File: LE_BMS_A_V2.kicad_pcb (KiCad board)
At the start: 4 copper layers, 80 x 80 mm, 56 parts, among them J1 10155435-00011LF, J2 CAN1, J3 691382010012, J4 691313510002, J5 RJHSE5380, J6 CAN1, U1 ESP32-S3-WROOM-2, U2 MCP2515-xST, U3 ISO1050DUB, U4 ISO1050DUB, U5 TLV1117LV33DCYT, U6 DS3231MZ, Y1 ABM3B-8.000MHZ-10-1-U-T

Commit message: Moved the PCB a bit.
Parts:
- added REF**: BatteryHolder_MYOUNG_BS-07-A1BJ001_CR2032, Battery:BatteryHolder_MYOUNG_BS-07-A1BJ001_CR2032, F.Cu at (127.2, 64.2)
- moved C5 70.8 mm to (180.1, 49.6)
- moved C6 70.8 mm to (166.1, 97.2)
- moved C7 70.8 mm to (136.1, 97.1)
- moved J6 70.8 mm to (171.3, 117.3)
- moved U2 70.8 mm to (133.1, 85.6)
- moved U4 70.8 mm to (130.3, 102.5)
- moved U6 70.8 mm to (153.4, 84.4)
- moved C1 70.8 mm to (151.8, 53.8)
- moved C10 70.8 mm to (145.7, 116.6)
- moved C12 70.8 mm to (133.2, 109.4)
- moved C13 70.8 mm to (139.0, 89.9)
- moved C14 70.8 mm to (139.0, 81.7)
- moved C15 70.8 mm to (175.0, 105.3)
- moved C17 70.8 mm to (175.0, 99.8)
- moved C18 70.8 mm to (138.8, 99.5)
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
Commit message: Finished most routing, final checks to be done
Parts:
- removed REF**: BatteryHolder_MYOUNG_BS-07-A1BJ001_CR2032, Battery:BatteryHolder_MYOUNG_BS-07-A1BJ001_CR2032
- added BT1: Battery_Cell, Battery:BatteryHolder_MYOUNG_BS-07-A1BJ001_CR2032, F.Cu at (118.1, 72.4)
- added G***: LOGO, LOGO, F.Cu at (137.7, 89.5)
- added J7: 691382010006, 691382010006:691382010006, F.Cu at (187.0, 84.1)
- J3: value 691382010012 -> 691382010006; footprint 691382010012:691382010012 -> 691382010006:691382010006
- moved C22 45.6 mm to (116.6, 95.3), turned to 180 degrees
- moved J1 41.4 mm to (141.3, 48.4), turned to 180 degrees
- moved C23 41.0 mm to (119.7, 85.6)
- moved U6 35.8 mm to (118.2, 90.4), turned to -90 degrees
- moved R4 32.5 mm to (138.6, 55.4), turned to 180 degrees
- moved R3 31.3 mm to (143.4, 55.4), turned to 180 degrees
- moved R11 29.3 mm to (117.9, 83.9), turned to 180 degrees
- moved R9 27.8 mm to (122.3, 94.9)
- moved R10 27.4 mm to (122.3, 96.5), turned to 180 degrees
- moved C8 23.8 mm to (152.0, 79.5), turned to 180 degrees
- moved S1 21.8 mm to (130.3, 51.2), turned to 180 degrees
- moved C14 17.1 mm to (153.9, 90.0), turned to -90 degrees
- moved U2 17.0 mm to (150.0, 84.0), turned to 0 degrees
- moved R2 16.2 mm to (130.3, 57.9), turned to 0 degrees
- moved C4 14.4 mm to (130.3, 56.4), turned to 180 degrees
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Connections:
- J3 pad 1: unconnected-(J3-Pad1) -> +5V
- J3 pad 2: unconnected-(J3-Pad2) -> GND
- J3 pad 3: unconnected-(J3-Pad3) -> /Project Architecture/Section A - Title A/GPIO_A1
- J3 pad 4: unconnected-(J3-Pad4) -> /Project Architecture/Section A - Title A/GPIO_A2
- J3 pad 5: unconnected-(J3-Pad5) -> /Project Architecture/Section A - Title A/GPIO_A3
- J3 pad 6: unconnected-(J3-Pad6) -> /Project Architecture/Section A - Title A/GPIO_A4
- R10 pad 2: /Project Architecture/Section A - Title A/SDA -> /Project Architecture/Section A - Title A/I2C_SDA
- R9 pad 1: /Project Architecture/Section A - Title A/SCL -> /Project Architecture/Section A - Title A/I2C_SCL
- U1 pad 12: unconnected-(U1-IO8-Pad12) -> /Project Architecture/Section A - Title A/I2C_SDA
- U1 pad 17: /Project Architecture/Section A - Title A/CAN2_INT -> /Project Architecture/Section A - Title A/I2C_SCL
- U1 pad 25: unconnected-(U1-IO48-Pad25) -> /Project Architecture/Section A - Title A/CAN2_INT
- U1 pad 35: unconnected-(U1-MTMS/IO42-Pad35) -> /Project Architecture/Section A - Title A/GPIO_A1
- U1 pad 36: unconnected-(U1-RXD0/IO44-Pad36) -> /Project Architecture/Section A - Title A/GPIO_A2
- U1 pad 37: unconnected-(U1-TXD0/IO43-Pad37) -> /Project Architecture/Section A - Title A/GPIO_A3
- U1 pad 38: unconnected-(U1-IO2-Pad38) -> /Project Architecture/Section A - Title A/GPIO_A4
- U1 pad 5: unconnected-(U1-IO5-Pad5) -> /Project Architecture/Section A - Title A/GPIO_B4
- U1 pad 6: unconnected-(U1-IO6-Pad6) -> /Project Architecture/Section A - Title A/GPIO_B3
- U1 pad 7: unconnected-(U1-IO7-Pad7) -> /Project Architecture/Section A - Title A/GPIO_B2
- U1 pad 8: unconnected-(U1-IO15-Pad8) -> /Project Architecture/Section A - Title A/GPIO_B1
- U6 pad 7: /Project Architecture/Section A - Title A/SDA -> /Project Architecture/Section A - Title A/I2C_SDA
- U6 pad 8: /Project Architecture/Section A - Title A/SCL -> /Project Architecture/Section A - Title A/I2C_SCL
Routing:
- net +5V: track 36.6 -> 143.3 mm, vias 0 -> 1
- net /Project Architecture/Section A - Title A/ESP32_BOOT: track 0.00 -> 54.9 mm, vias 0 -> 2
- net /Project Architecture/Section A - Title A/I2C_SDA: track 0.00 -> 53.2 mm, vias 0 -> 2
- net /Project Architecture/Section A - Title A/I2C_SCL: track 0.00 -> 52.1 mm
- net /Project Architecture/Section A - Title A/GPIO_B1: track 0.00 -> 46.2 mm, vias 0 -> 1
- net /Project Architecture/Section A - Title A/GPIO_B2: track 0.00 -> 45.2 mm, vias 0 -> 1
- net /Project Architecture/Section A - Title A/GPIO_B3: track 0.00 -> 44.6 mm, vias 0 -> 1
- net /Project Architecture/Section A - Title A/GPIO_B4: track 0.00 -> 44.4 mm, vias 0 -> 1
- net /Project Architecture/Section A - Title A/ESP32_EN: track 0.00 -> 42.1 mm, vias 0 -> 2
- net GND: track 19.9 -> 59.0 mm, vias 14 -> 39
- net /Project Architecture/Section A - Title A/CAN1_TX: track 0.00 -> 29.7 mm, vias 0 -> 2
- net /Project Architecture/Section A - Title A/CAN1_RX: track 0.00 -> 28.1 mm
- net /Project Architecture/Section B - Title B/CAN2_TX: track 0.00 -> 28.1 mm
- net /Project Architecture/Section B - Title B/CAN2_RX: track 0.00 -> 25.7 mm
- net /Project Architecture/Section A - Title A/ESP32_USB_D+: track 5.03 -> 28.5 mm
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- added copper zone on In2.Cu, net +5V_CAN2
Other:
- board text added: "16/05/26"
- board text added: "3.0V CR2032"
- board text added: "Central Unit"
- board text added: "LE_BMS_A_V2"
- board text added: "V0R1"
- board text added: "www.cusmith.tech"

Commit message: Final Changes, Updated to Checked
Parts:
- BT1: value Battery_Cell -> CR2032
- C1, C3: value 1u -> 1uF
- C15, C16, C17, C18, C19, C20, C21: value C -> 1uF
- C2, C4: value 0.1u -> 0.1uF
- moved D1 3.75 mm to (180.4, 52.1), turned to -90 degrees
- moved C5 3.11 mm to (182.9, 52.1), turned to 90 degrees
- moved S1 2.25 mm to (132.6, 51.1)
- moved C4 2.25 mm to (132.6, 56.4)
- moved R2 2.25 mm to (132.6, 57.9)
- moved R4 2.23 mm to (140.8, 55.4)
- moved J1 2.23 mm to (143.5, 48.4)
- moved R3 2.23 mm to (145.6, 55.4)
- moved C2 1.30 mm to (125.5, 56.3)
- moved R1 1.30 mm to (125.5, 57.8)
- moved S2 1.30 mm to (125.5, 51.1)
- moved C17 0.17 mm to (175.1, 99.7)
- moved J4 0.11 mm to (186.0, 102.7)
- moved U5 0.07 mm to (174.3, 88.7)
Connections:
- net /Project Architecture/Section A - Title A/I2C_SCL renamed /Project Architecture/Section D - RTC/I2C_SCL
- net /Project Architecture/Section A - Title A/I2C_SDA renamed /Project Architecture/Section D - RTC/I2C_SDA
- net /Project Architecture/Section A - Title A/RTC_INT renamed /Project Architecture/Section D - RTC/RTC_INT
- net /Project Architecture/Section A - Title A/RTC_RST renamed /Project Architecture/Section D - RTC/RTC_RST
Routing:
- net +5V: track 143.3 -> 130.7 mm
- net /Project Architecture/Section A - Title A/ESP32_BOOT: track 54.9 -> 52.7 mm
- net /Project Architecture/Section A - Title A/ESP32_EN: track 42.1 -> 40.8 mm
- net /Project Architecture/Section A - Title A/ESP32_USB_D-: track 27.8 -> 26.9 mm
- net /Project Architecture/Section A - Title A/ESP32_USB_D+: track 28.5 -> 27.6 mm
- net GND_CAN1: track 28.3 -> 27.7 mm
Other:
- board text added: "3.0V CR2032 ONLY"
- board text added: "BOOT"
- board text added: "EN"
- board text added: "GPIOA"
- board text added: "GPIOB"
- board text added: "LE"
- board text removed: "3.0V CR2032"

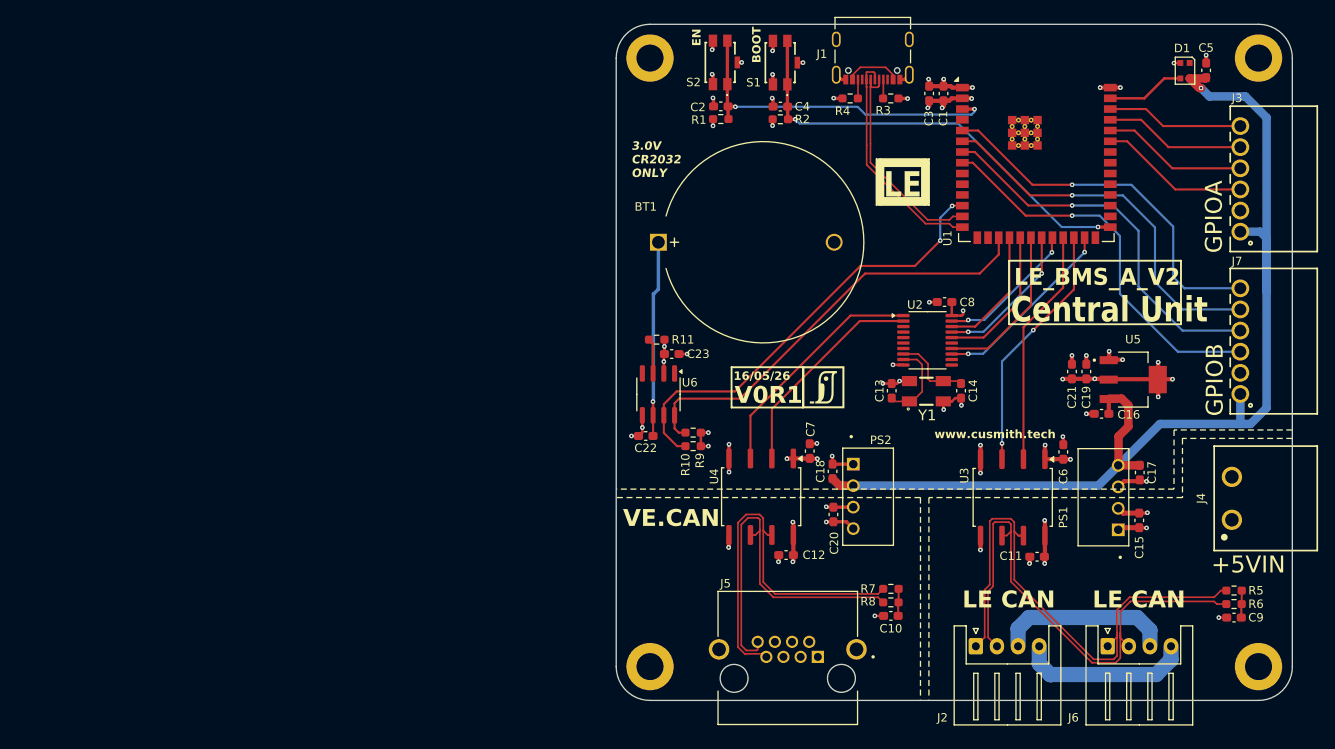
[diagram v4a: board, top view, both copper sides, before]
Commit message: Increased Via Sizes to 0.3/0.6
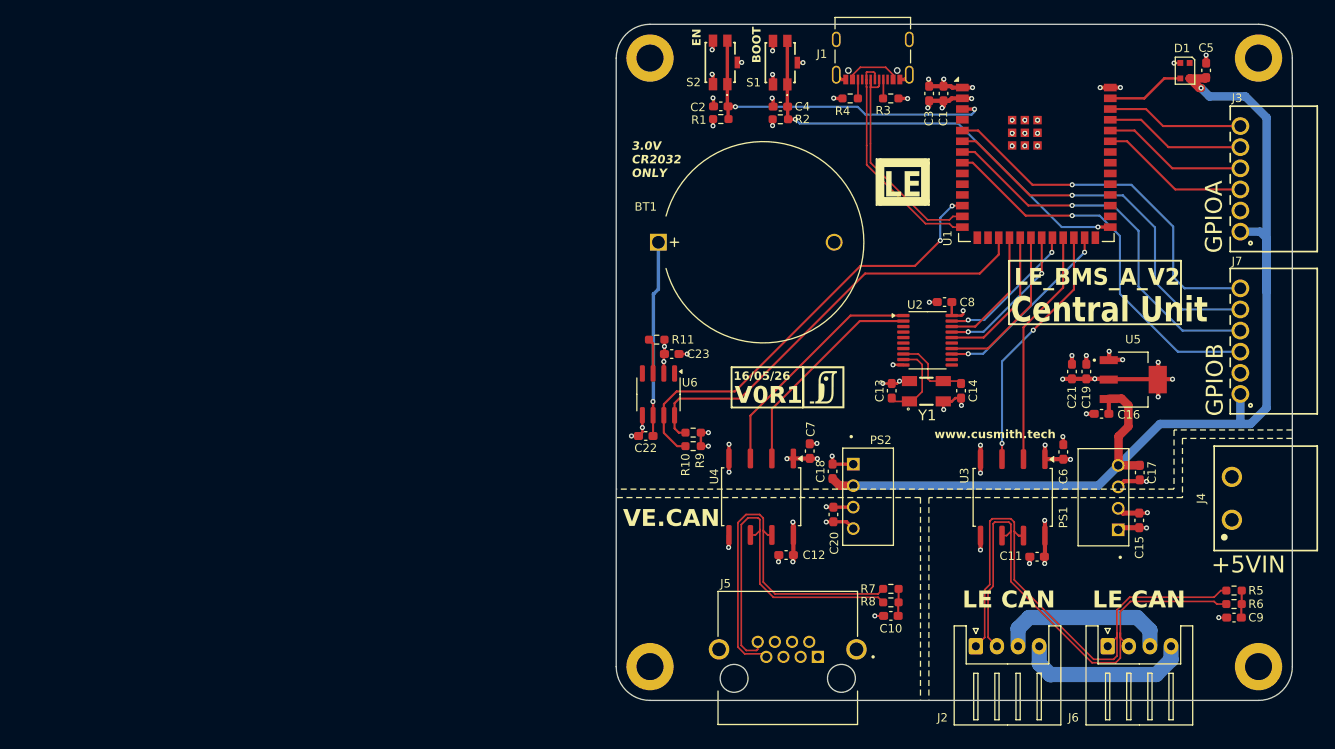
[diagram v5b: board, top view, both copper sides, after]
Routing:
- net GND: vias 39 -> 48

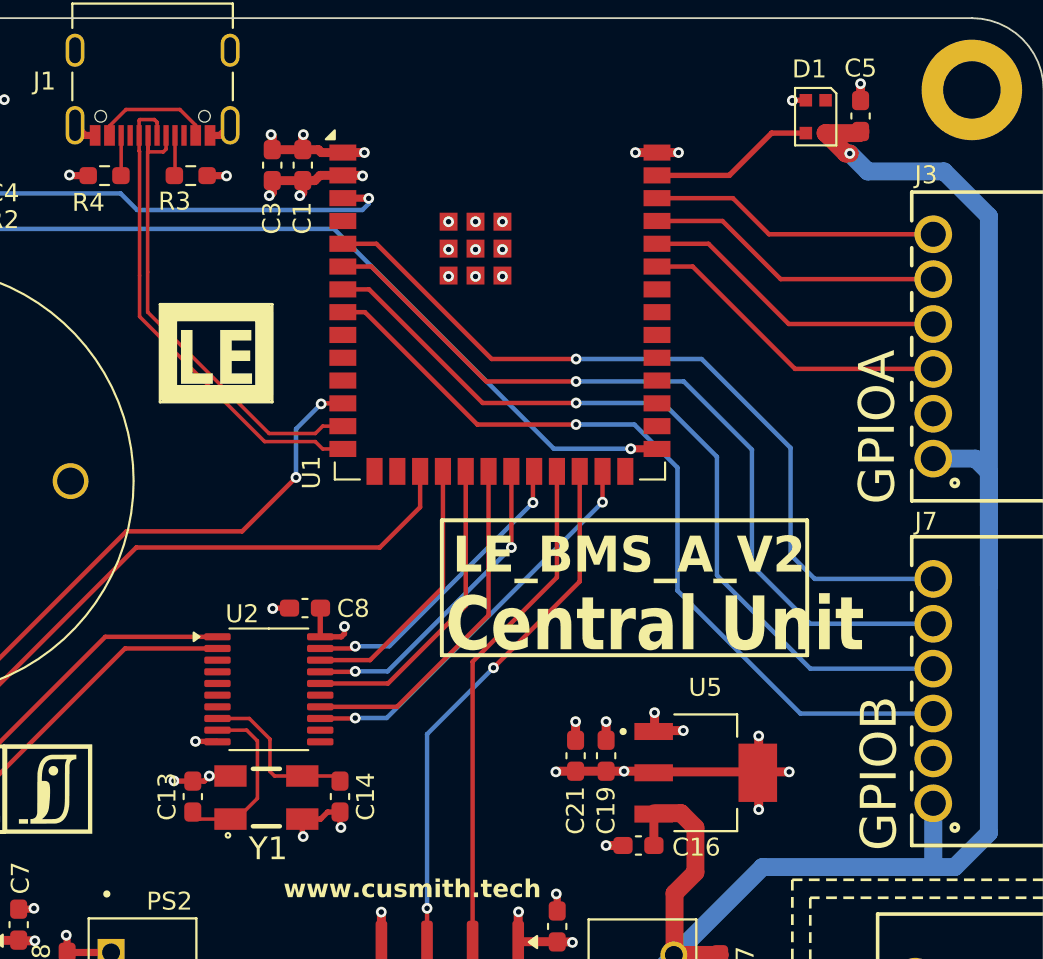
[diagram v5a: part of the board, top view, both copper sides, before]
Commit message: Added pulldowns on GPIOs
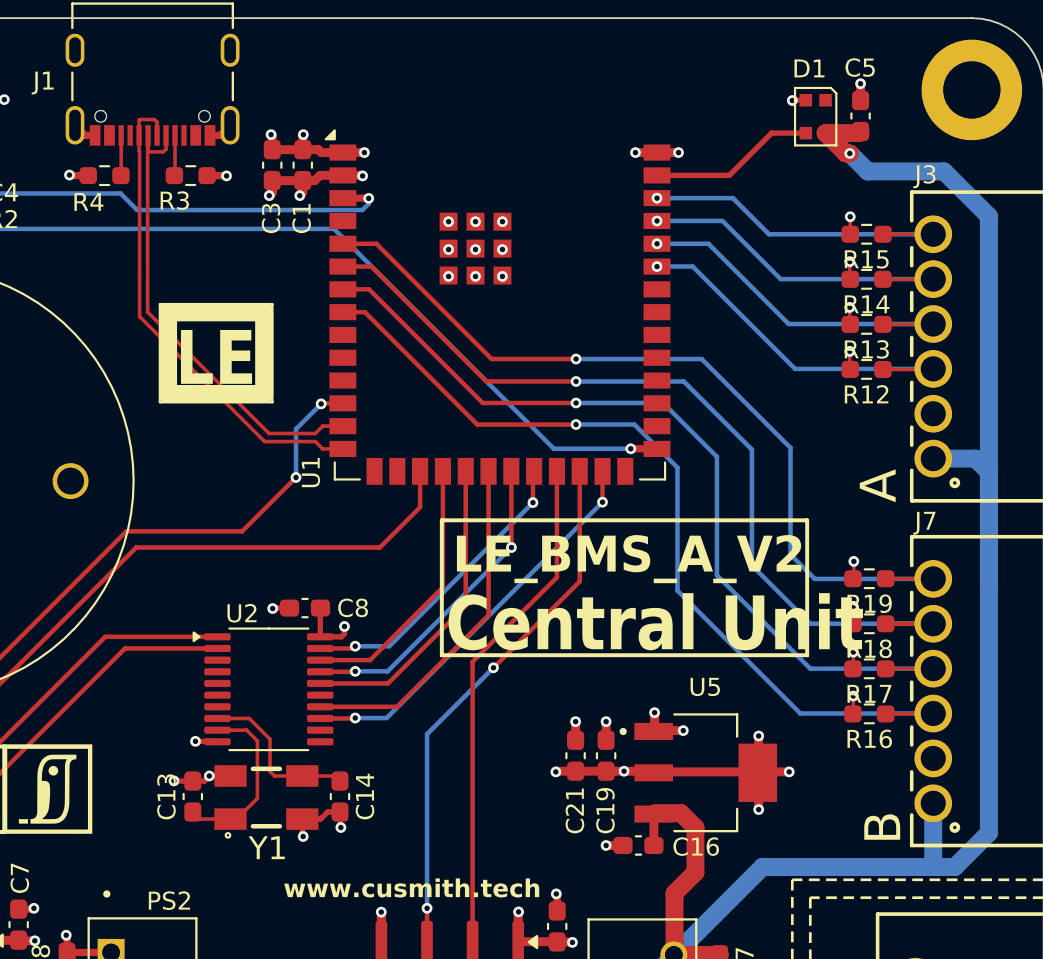
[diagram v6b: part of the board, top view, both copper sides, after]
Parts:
- added R12: 10k, Resistor_SMD:R_0603_1608Metric_Pad0.98x0.95mm_HandSolder, F.Cu at (183.3, 66.2)
- added R13: 10k, Resistor_SMD:R_0603_1608Metric_Pad0.98x0.95mm_HandSolder, F.Cu at (183.3, 63.7)
- added R14: 10k, Resistor_SMD:R_0603_1608Metric_Pad0.98x0.95mm_HandSolder, F.Cu at (183.3, 61.2)
- added R15: 10k, Resistor_SMD:R_0603_1608Metric_Pad0.98x0.95mm_HandSolder, F.Cu at (183.3, 58.6)
- added R16: 10k, Resistor_SMD:R_0603_1608Metric_Pad0.98x0.95mm_HandSolder, F.Cu at (183.4, 85.4)
- added R17: 10k, Resistor_SMD:R_0603_1608Metric_Pad0.98x0.95mm_HandSolder, F.Cu at (183.4, 82.9)
- added R18: 10k, Resistor_SMD:R_0603_1608Metric_Pad0.98x0.95mm_HandSolder, F.Cu at (183.4, 80.3)
- added R19: 10k, Resistor_SMD:R_0603_1608Metric_Pad0.98x0.95mm_HandSolder, F.Cu at (183.4, 77.8)
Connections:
- J1 pad A4_B9: VBUS -> unconnected-(J1-VBUS-PadA4_B9)
- J1 pad B4_A9: VBUS -> unconnected-(J1-VBUS-PadA4_B9)_1
- U6 pad 4: /Project Architecture/Section D - RTC/RTC_RST -> unconnected-(U6-~{RST}-Pad4)
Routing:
- net GND: track 59.2 -> 67.0 mm, vias 48 -> 56
- net VBUS: track 6.64 -> 0.00 mm
- net /Project Architecture/Section A - Title A/GPIO_A1: track 17.8 -> 20.6 mm, vias 0 -> 1
- net /Project Architecture/Section A - Title A/GPIO_A2: track 17.2 -> 20.0 mm, vias 0 -> 1
- net /Project Architecture/Section A - Title A/GPIO_A3: track 16.7 -> 19.5 mm, vias 0 -> 1
- net /Project Architecture/Section A - Title A/GPIO_A4: track 16.2 -> 19.0 mm, vias 0 -> 1
- net /Project Architecture/Section A - Title A/GPIO_B1: track 46.2 -> 48.8 mm
- net /Project Architecture/Section A - Title A/GPIO_B2: track 45.5 -> 48.2 mm
- net /Project Architecture/Section A - Title A/GPIO_B4: track 44.1 -> 46.8 mm
- net /Project Architecture/Section A - Title A/GPIO_B3: track 44.9 -> 47.6 mm
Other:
- board text added: "A"
- board text added: "B"
- board text removed: "GPIOA"
- board text removed: "GPIOB"
